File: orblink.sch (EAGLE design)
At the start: 13 parts, among them U1 ATTINY

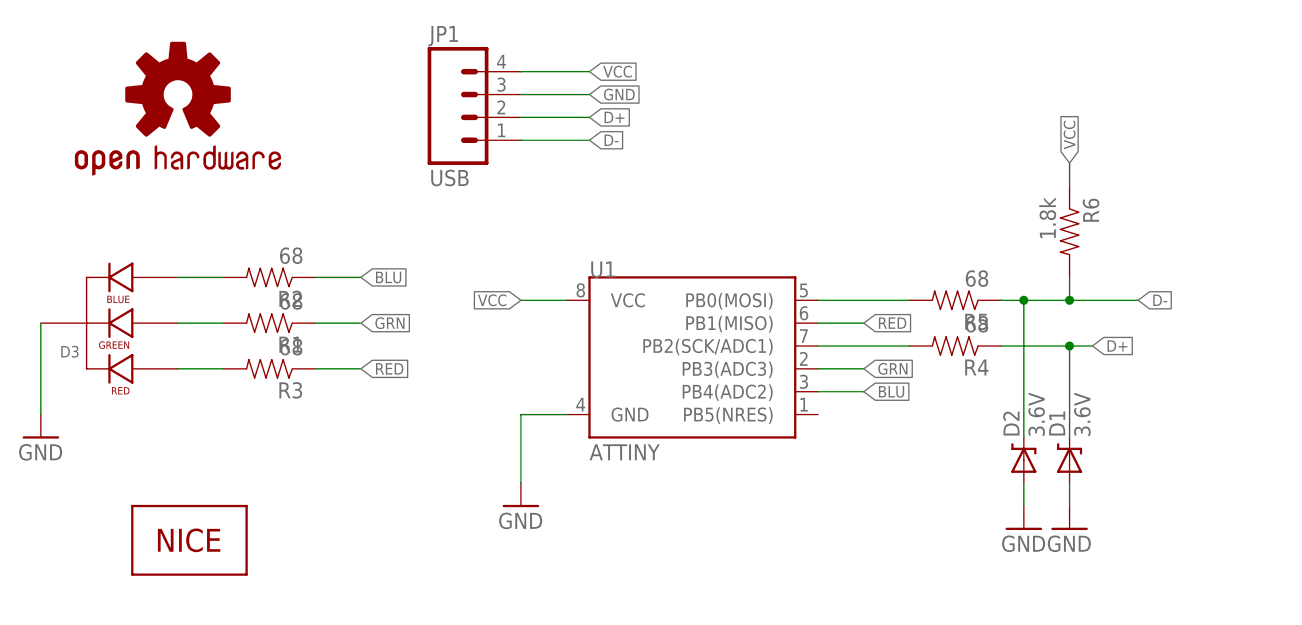
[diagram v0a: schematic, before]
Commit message: Switched LED and USB pin
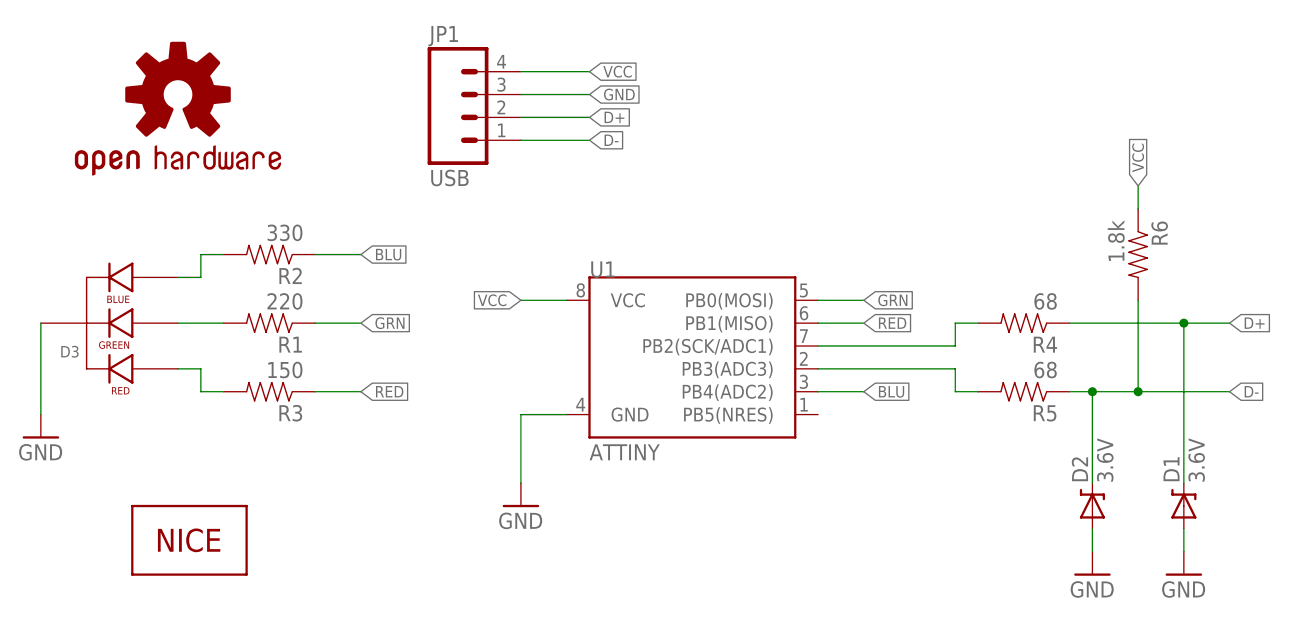
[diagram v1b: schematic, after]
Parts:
- R1: value 68 -> 220
- R2: value 68 -> 330
- R3: value 68 -> 150
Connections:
- net GRN: now also U1.PB0(MOSI); no longer U1.PB3(ADC3)
- net N$4: now also U1.PB3(ADC3); no longer U1.PB0(MOSI)
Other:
- moved on the sheet: D1, D2, R2, R3, R4, R5, R6
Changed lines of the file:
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@@
 <part name="GND2" library="supply1" deviceset="GND" device=""/>
 <part name="GND3" library="supply1" deviceset="GND" device=""/>
-<part name="R2" library="SparkFun-Resistors" deviceset="RESISTOR" device="PTH-1/6W" value="68"/>
-<part name="R1" library="SparkFun-Resistors" deviceset="RESISTOR" device="PTH-1/6W" value="68"/>
-<part name="R3" library="SparkFun-Resistors" deviceset="RESISTOR" device="PTH-1/6W" value="68"/>
+<part name="R2" library="SparkFun-Resistors" deviceset="RESISTOR" device="PTH-1/6W" value="330"/>
+<part name="R1" library="SparkFun-Resistors" deviceset="RESISTOR" device="PTH-1/6W" value="220"/>
+<part name="R3" library="SparkFun-Resistors" deviceset="RESISTOR" device="PTH-1/6W" value="150"/>
 <part name="GND4" library="supply1" deviceset="GND" device=""/>
 <part name="D3" library="SparkFun-LED" deviceset="LED-RGB-CC-THRU" device="DIFFUSE"/>
@@
 <instances>
 <instance part="U1" gate="G$1" x="53.34" y="48.26"/>
-<instance part="R5" gate="G$1" x="81.28" y="55.88" rot="R180"/>
+<instance part="R5" gate="G$1" x="88.9" y="45.72" rot="R180"/>
 <instance part="GND1" gate="1" x="33.02" y="33.02"/>
-<instance part="R4" gate="G$1" x="81.28" y="50.8" rot="R180"/>
-<instance part="R6" gate="G$1" x="93.98" y="63.5" rot="R270"/>
-<instance part="D2" gate="G$1" x="88.9" y="38.1" rot="R90"/>
-<instance part="D1" gate="G$1" x="93.98" y="38.1" rot="R90"/>
-<instance part="GND2" gate="1" x="88.9" y="30.48"/>
-<instance part="GND3" gate="1" x="93.98" y="30.48"/>
-<instance part="R2" gate="G$1" x="5.08" y="58.42" rot="R180"/>
+<instance part="R4" gate="G$1" x="88.9" y="53.34" rot="R180"/>
+<instance part="R6" gate="G$1" x="101.6" y="60.96" rot="R270"/>
+<instance part="D2" gate="G$1" x="96.52" y="33.02" rot="R90"/>
+<instance part="D1" gate="G$1" x="106.68" y="33.02" rot="R90"/>
+<instance part="GND2" gate="1" x="96.52" y="25.4"/>
+<instance part="GND3" gate="1" x="106.68" y="25.4"/>
+<instance part="R2" gate="G$1" x="5.08" y="60.96" rot="R180"/>
 <instance part="R1" gate="G$1" x="5.08" y="53.34" rot="R180"/>
-<instance part="R3" gate="G$1" x="5.08" y="48.26" rot="R180"/>
+<instance part="R3" gate="G$1" x="5.08" y="45.72" rot="R180"/>
 <instance part="GND4" gate="1" x="-20.32" y="40.64"/>
 <instance part="D3" gate="G$1" x="-10.16" y="53.34" rot="R180"/>
@@
 <pinref part="D2" gate="G$1" pin="A"/>
 <pinref part="GND2" gate="1" pin="GND"/>
-<wire x1="88.9" y1="35.56" x2="88.9" y2="33.02" width="0.1524" layer="91"/>
+<wire x1="96.52" y1="30.48" x2="96.52" y2="27.94" width="0.1524" layer="91"/>
 </segment>
 <segment>
 <pinref part="D1" gate="G$1" pin="A"/>
 <pinref part="GND3" gate="1" pin="GND"/>
-<wire x1="93.98" y1="35.56" x2="93.98" y2="33.02" width="0.1524" layer="91"/>
+<wire x1="106.68" y1="30.48" x2="106.68" y2="27.94" width="0.1524" layer="91"/>
 </segment>
 <segment>
@@
 <segment>
 <pinref part="R4" gate="G$1" pin="1"/>
-<wire x1="86.36" y1="50.8" x2="93.98" y2="50.8" width="0.1524" layer="91"/>
-<label x="96.52" y="50.8" size="1.27" layer="95" xref="yes"/>
+<wire x1="93.98" y1="53.34" x2="106.68" y2="53.34" width="0.1524" layer="91"/>
+<label x="111.76" y="53.34" size="1.27" layer="95" xref="yes"/>
 <pinref part="D1" gate="G$1" pin="C"/>
-<wire x1="93.98" y1="50.8" x2="96.52" y2="50.8" width="0.1524" layer="91"/>
-<wire x1="93.98" y1="40.64" x2="93.98" y2="50.8" width="0.1524" layer="91"/>
-<junction x="93.98" y="50.8"/>
+<wire x1="106.68" y1="53.34" x2="111.76" y2="53.34" width="0.1524" layer="91"/>
+<wire x1="106.68" y1="35.56" x2="106.68" y2="53.34" width="0.1524" layer="91"/>
+<junction x="106.68" y="53.34"/>
 </segment>
 <segment>
@@
 <pinref part="U1" gate="G$1" pin="PB2(SCK/ADC1)"/>
 <pinref part="R4" gate="G$1" pin="2"/>
-<wire x1="66.04" y1="50.8" x2="76.2" y2="50.8" width="0.1524" layer="91"/>
-</segment>
-</net>
-<net name="N$4" class="0">
-<segment>
-<pinref part="U1" gate="G$1" pin="PB0(MOSI)"/>
-<pinref part="R5" gate="G$1" pin="2"/>
-<wire x1="66.04" y1="55.88" x2="76.2" y2="55.88" width="0.1524" layer="91"/>
+<wire x1="66.04" y1="50.8" x2="81.28" y2="50.8" width="0.1524" layer="91"/>
+<wire x1="81.28" y1="50.8" x2="81.28" y2="53.34" width="0.1524" layer="91"/>
+<wire x1="81.28" y1="53.34" x2="83.82" y2="53.34" width="0.1524" layer="91"/>
 </segment>
 </net>
@@
 <segment>
 <pinref part="R5" gate="G$1" pin="1"/>
-<wire x1="86.36" y1="55.88" x2="88.9" y2="55.88" width="0.1524" layer="91"/>
+<wire x1="93.98" y1="45.72" x2="96.52" y2="45.72" width="0.1524" layer="91"/>
 <pinref part="R6" gate="G$1" pin="2"/>
-<wire x1="88.9" y1="55.88" x2="93.98" y2="55.88" width="0.1524" layer="91"/>
-<wire x1="93.98" y1="55.88" x2="101.6" y2="55.88" width="0.1524" layer="91"/>
-<wire x1="93.98" y1="58.42" x2="93.98" y2="55.88" width="0.1524" layer="91"/>
-<junction x="93.98" y="55.88"/>
-<label x="101.6" y="55.88" size="1.27" layer="95" xref="yes"/>
+<wire x1="96.52" y1="45.72" x2="101.6" y2="45.72" width="0.1524" layer="91"/>
+<wire x1="101.6" y1="45.72" x2="111.76" y2="45.72" width="0.1524" layer="91"/>
+<wire x1="101.6" y1="55.88" x2="101.6" y2="45.72" width="0.1524" layer="91"/>
+<junction x="101.6" y="45.72"/>
+<label x="111.76" y="45.72" size="1.27" layer="95" xref="yes"/>
 <pinref part="D2" gate="G$1" pin="C"/>
-<wire x1="88.9" y1="40.64" x2="88.9" y2="55.88" width="0.1524" layer="91"/>
-<junction x="88.9" y="55.88"/>
+<wire x1="96.52" y1="35.56" x2="96.52" y2="45.72" width="0.1524" layer="91"/>
+<junction x="96.52" y="45.72"/>
 </segment>
 <segment>
@@
 <segment>
 <pinref part="R6" gate="G$1" pin="1"/>
-<wire x1="93.98" y1="68.58" x2="93.98" y2="71.12" width="0.1524" layer="91"/>
-<label x="93.98" y="71.12" size="1.27" layer="95" rot="R90" xref="yes"/>
+<wire x1="101.6" y1="66.04" x2="101.6" y2="68.58" width="0.1524" layer="91"/>
+<label x="101.6" y="68.58" size="1.27" layer="95" rot="R90" xref="yes"/>
 </segment>
 <segment>
@@
 <segment>
 <pinref part="R3" gate="G$1" pin="1"/>
-<wire x1="10.16" y1="48.26" x2="15.24" y2="48.26" width="0.1524" layer="91"/>
-<label x="15.24" y="48.26" size="1.27" layer="95" xref="yes"/>
+<wire x1="10.16" y1="45.72" x2="15.24" y2="45.72" width="0.1524" layer="91"/>
+<label x="15.24" y="45.72" size="1.27" layer="95" xref="yes"/>
 </segment>
 </net>
 <net name="GRN" class="0">
 <segment>
-<pinref part="U1" gate="G$1" pin="PB3(ADC3)"/>
-<wire x1="66.04" y1="48.26" x2="71.12" y2="48.26" width="0.1524" layer="91"/>
-<label x="71.12" y="48.26" size="1.27" layer="95" xref="yes"/>
-</segment>
-<segment>
 <pinref part="R1" gate="G$1" pin="1"/>
 <wire x1="10.16" y1="53.34" x2="15.24" y2="53.34" width="0.1524" layer="91"/>
 <label x="15.24" y="53.34" size="1.27" layer="95" xref="yes"/>
+</segment>
+<segment>
+<pinref part="U1" gate="G$1" pin="PB0(MOSI)"/>
+<wire x1="66.04" y1="55.88" x2="71.12" y2="55.88" width="0.1524" layer="91"/>
+<label x="71.12" y="55.88" size="1.27" layer="95" xref="yes"/>
 </segment>
 </net>
@@
 <segment>
 <pinref part="R2" gate="G$1" pin="1"/>
-<wire x1="10.16" y1="58.42" x2="15.24" y2="58.42" width="0.1524" layer="91"/>
-<label x="15.24" y="58.42" size="1.27" layer="95" xref="yes"/>
+<wire x1="10.16" y1="60.96" x2="15.24" y2="60.96" width="0.1524" layer="91"/>
+<label x="15.24" y="60.96" size="1.27" layer="95" xref="yes"/>
 </segment>
 </net>
@@
 <pinref part="D3" gate="G$1" pin="BLUE_CATHODE"/>
 <pinref part="R2" gate="G$1" pin="2"/>
-<wire x1="-5.08" y1="58.42" x2="0" y2="58.42" width="0.1524" layer="91"/>
+<wire x1="-5.08" y1="58.42" x2="-2.54" y2="58.42" width="0.1524" layer="91"/>
+<wire x1="-2.54" y1="58.42" x2="-2.54" y2="60.96" width="0.1524" layer="91"/>
+<wire x1="-2.54" y1="60.96" x2="0" y2="60.96" width="0.1524" layer="91"/>
 </segment>
 </net>
@@
 <pinref part="D3" gate="G$1" pin="RED_CATHODE"/>
 <pinref part="R3" gate="G$1" pin="2"/>
-<wire x1="-5.08" y1="48.26" x2="0" y2="48.26" width="0.1524" layer="91"/>
+<wire x1="-5.08" y1="48.26" x2="-2.54" y2="48.26" width="0.1524" layer="91"/>
+<wire x1="-2.54" y1="48.26" x2="-2.54" y2="45.72" width="0.1524" layer="91"/>
+<wire x1="-2.54" y1="45.72" x2="0" y2="45.72" width="0.1524" layer="91"/>
 </segment>
 </net>
+<net name="N$4" class="0">
+<segment>
+<pinref part="U1" gate="G$1" pin="PB3(ADC3)"/>
+<wire x1="66.04" y1="48.26" x2="81.28" y2="48.26" width="0.1524" layer="91"/>
+<wire x1="81.28" y1="48.26" x2="81.28" y2="45.72" width="0.1524" layer="91"/>
+<pinref part="R5" gate="G$1" pin="2"/>
+<wire x1="81.28" y1="45.72" x2="83.82" y2="45.72" width="0.1524" layer="91"/>
+</segment>
+</net>
